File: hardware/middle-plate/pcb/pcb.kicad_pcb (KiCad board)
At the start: 2 copper layers, 218 x 205.7 mm, 101 parts, among them J1 Conn_01x06, J2 Conn_01x06, J3 Conn_01x05, J4 Conn_01x04, SW1 MT-0-102-A101-M200-RS+PJ, SW10 TS4535TP 250GF 009, SW11 TS4535TP 250GF 009, SW2 TS4535TP 250GF 009, SW3 TS4535TP 250GF 009, SW4 TS4535TP 250GF 009, SW5 TS4535TP 250GF 009, SW6 TS4535TP 250GF 009, SW7 TS4535TP 250GF 009, SW8 TS4535TP 250GF 009, SW9 TS4535TP 250GF 009, U1 Pico, U2 RPi_Zero_2W, U3 SN74LVC1T45DBV, U4 MAX98357_breakout

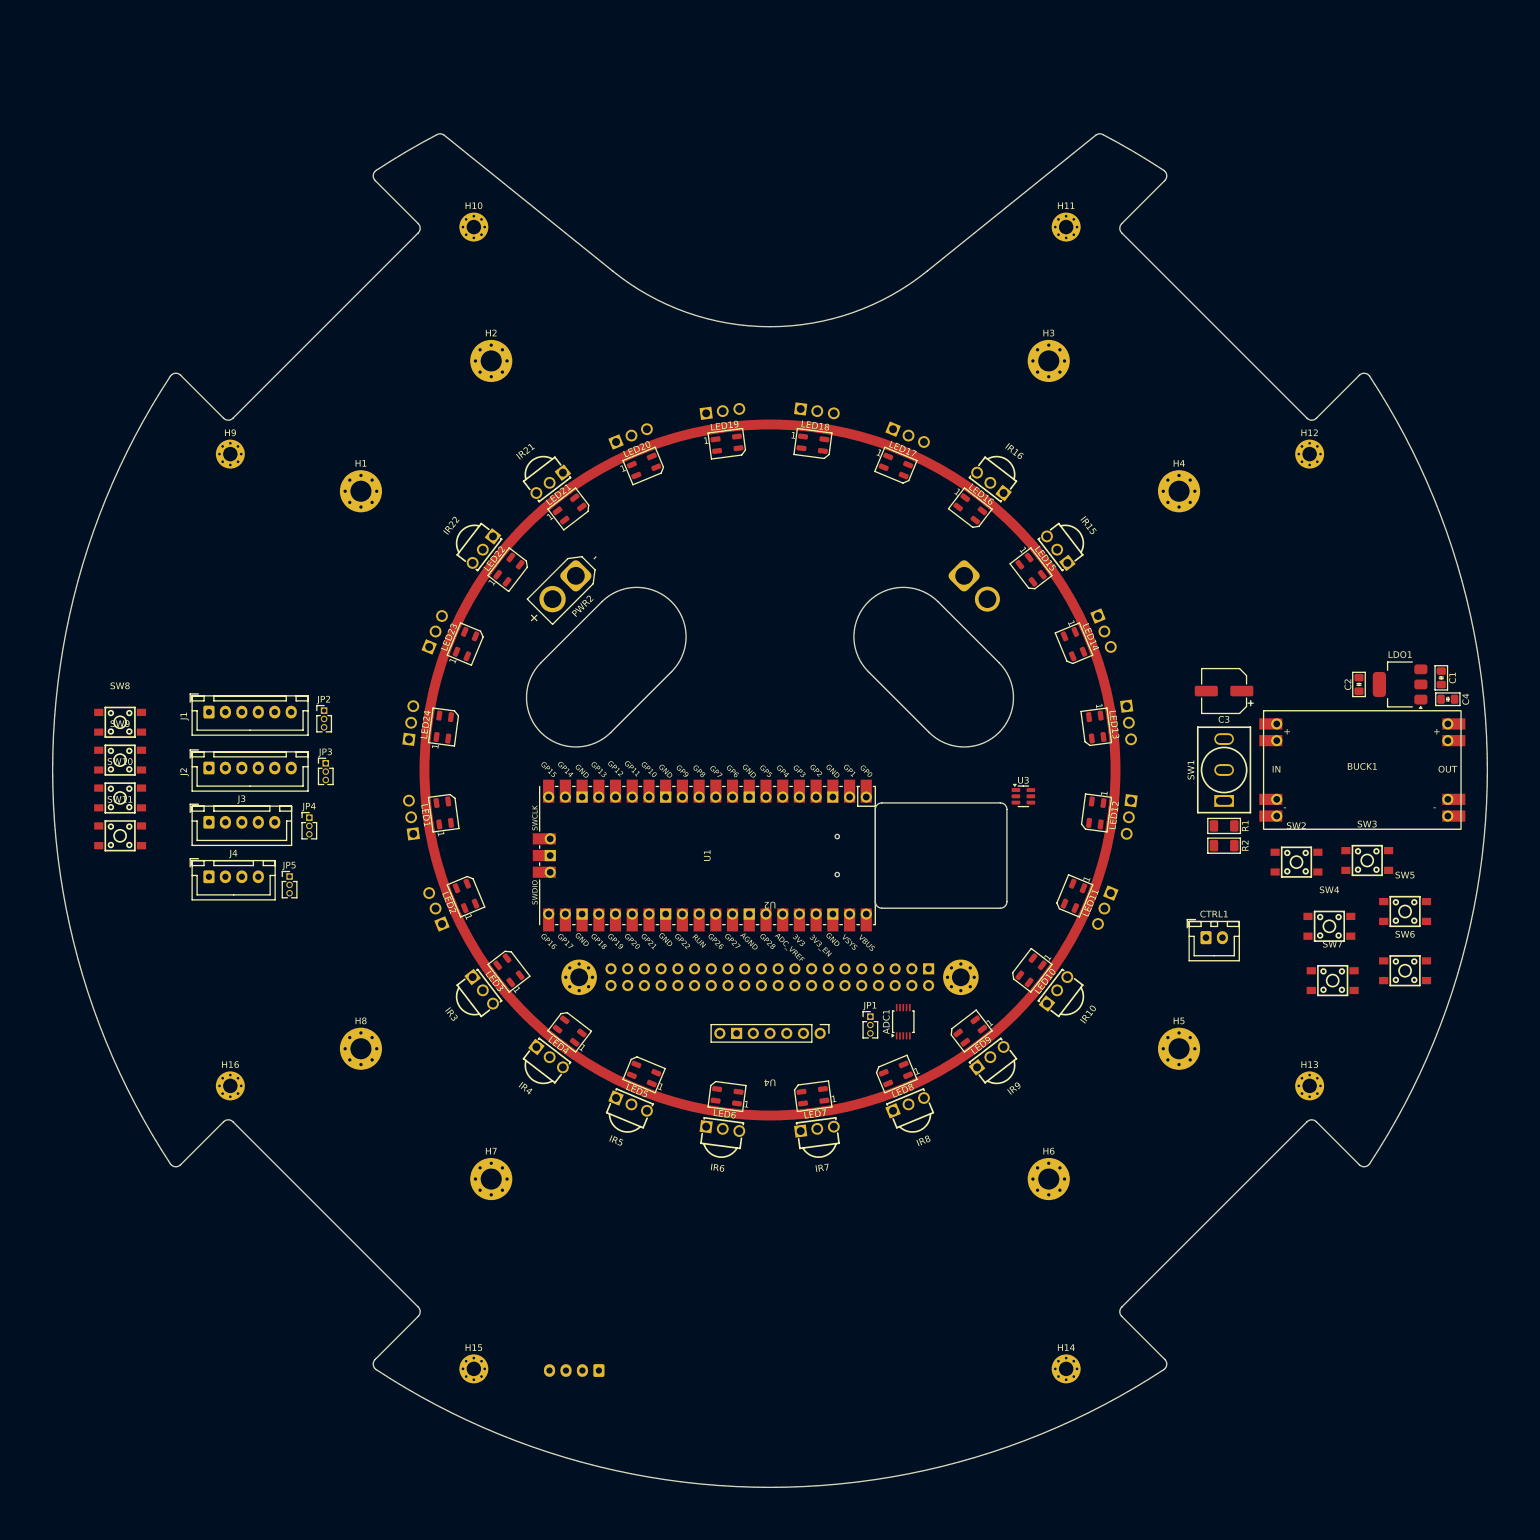
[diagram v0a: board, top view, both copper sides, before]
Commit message: middle plate completed other than cutouts
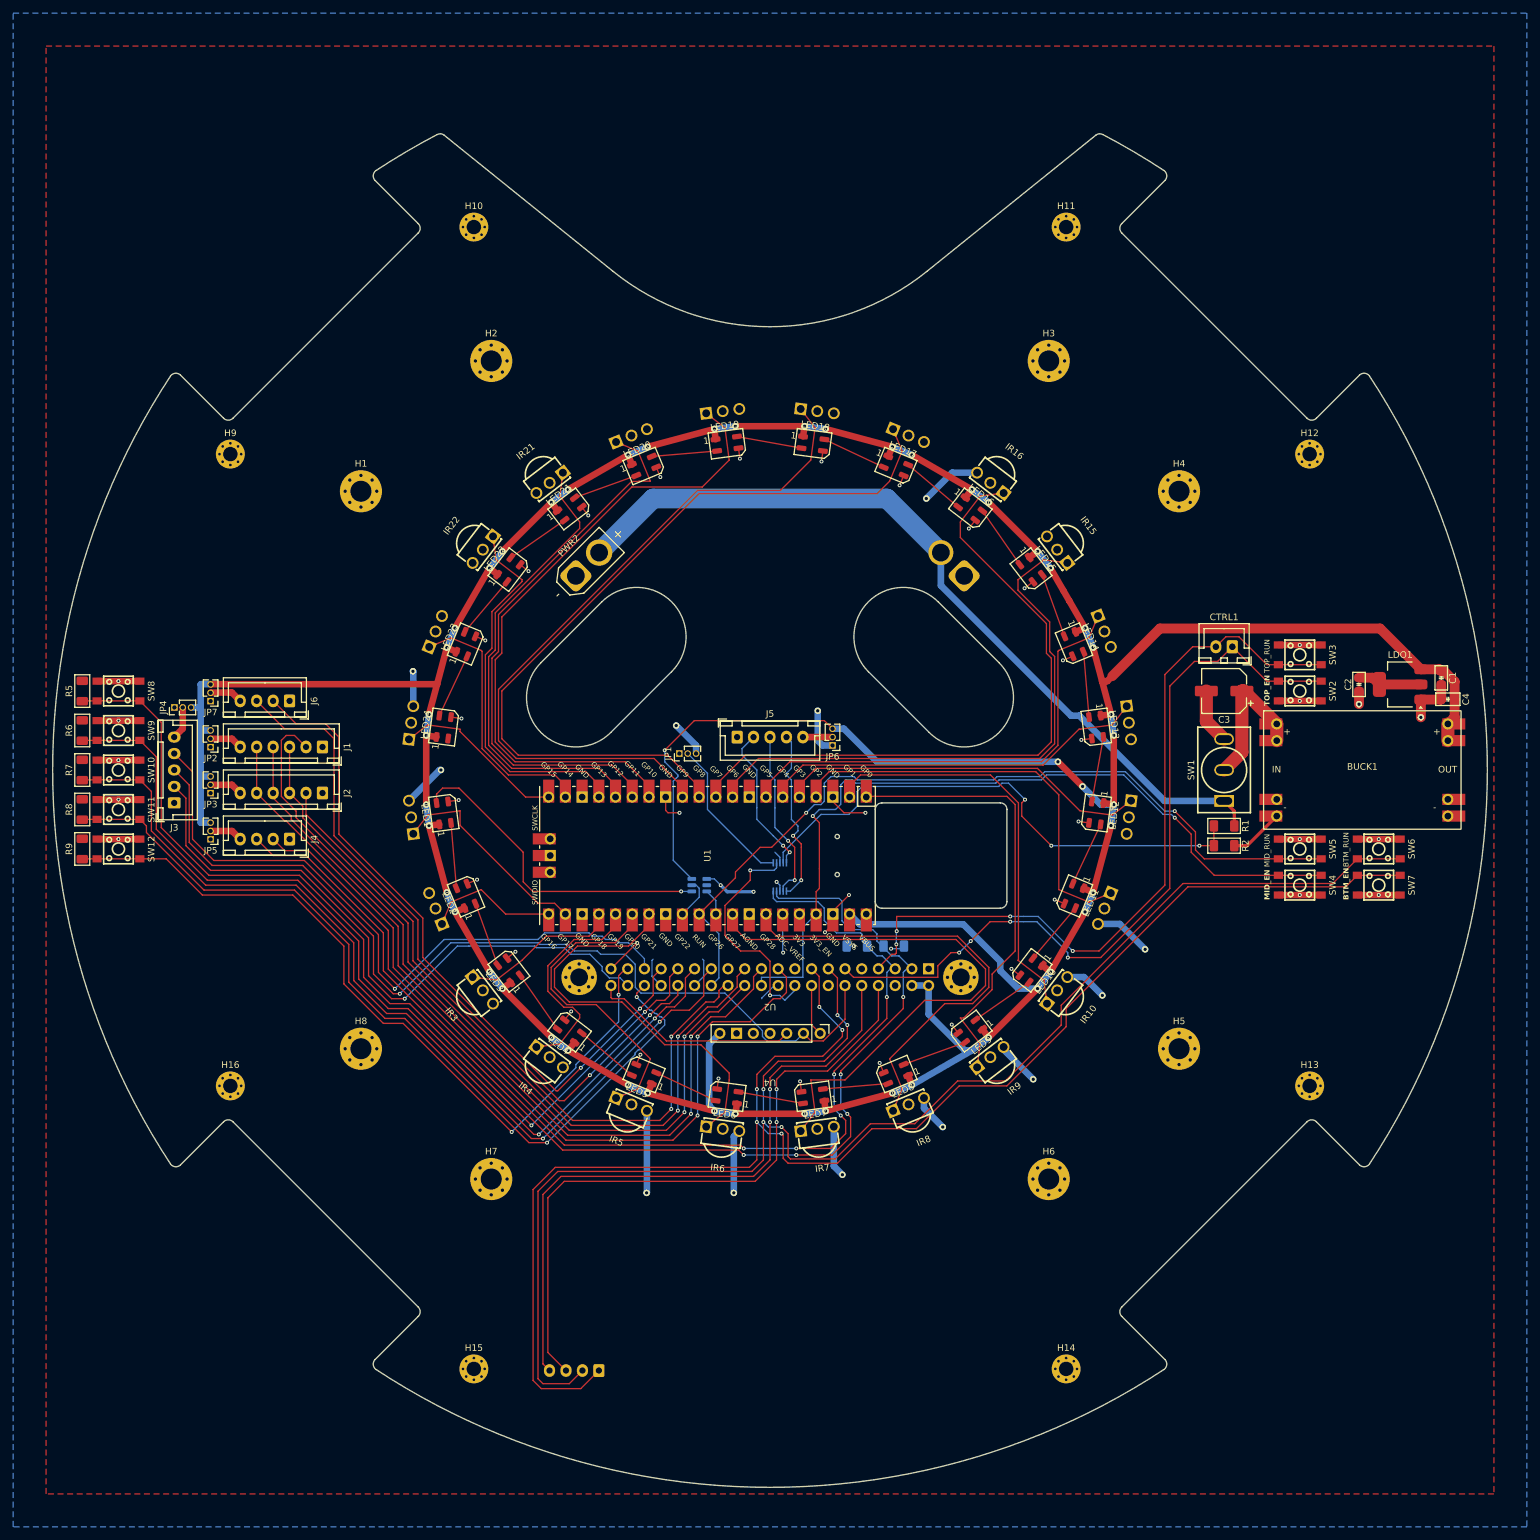
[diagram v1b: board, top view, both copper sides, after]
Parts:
- added J5: Conn_01x05, Connector_JST:JST_XH_B5B-XH-A_1x05_P2.50mm_Vertical, F.Cu at (-5.00, -5.00)
- added J6: Conn_01x04, Connector_JST:JST_XH_B4B-XH-A_1x04_P2.50mm_Vertical, F.Cu at (-73.0, -10.5)
- added JP6: Jumper_3_Bridged12, Connector_PinHeader_1.27mm:PinHeader_1x03_P1.27mm_Vertical, F.Cu at (9.50, -3.73)
- added JP7: Jumper_3_Bridged12, Connector_PinHeader_1.27mm:PinHeader_1x03_P1.27mm_Vertical, F.Cu at (-85.0, -10.5)
- added R3: 2.7kR, PCM_Resistor_SMD_AKL:R_1206_3216Metric_Pad1.30x1.75mm_HandSolder, B.Cu at (18.8, 26.8)
- added R4: 2.7kR, PCM_Resistor_SMD_AKL:R_1206_3216Metric_Pad1.30x1.75mm_HandSolder, B.Cu at (13.2, 26.8)
- added R5: 10kR, PCM_Resistor_SMD_AKL:R_1206_3216Metric_Pad1.30x1.75mm_HandSolder, F.Cu at (-104.5, -12.0)
- added R6: 10kR, PCM_Resistor_SMD_AKL:R_1206_3216Metric_Pad1.30x1.75mm_HandSolder, F.Cu at (-104.5, -6.00)
- added R7: 10kR, PCM_Resistor_SMD_AKL:R_1206_3216Metric_Pad1.30x1.75mm_HandSolder, F.Cu at (-104.5, 0.00)
- added R8: 10kR, PCM_Resistor_SMD_AKL:R_1206_3216Metric_Pad1.30x1.75mm_HandSolder, F.Cu at (-104.5, 6.00)
- added R9: 10kR, PCM_Resistor_SMD_AKL:R_1206_3216Metric_Pad1.30x1.75mm_HandSolder, F.Cu at (-104.5, 12.0)
- added SW12: TS4535TP 250GF 009, EasyEDA:SW-SMD_4P-L4.5-W4.5-P3.00-LS6.8, F.Cu at (-99.0, 12.0)
- ADC1, U3: moved to B.Cu
- moved U3 51.1 mm to (-10.8, 17.5), turned to 180 degrees
- moved JP1 49.4 mm to (-13.8, -2.50), turned to 90 degrees
- moved CTRL1 44.4 mm to (70.2, -18.7), turned to 180 degrees
- moved SW3 32.9 mm to (80.5, -17.5)
- moved ADC1 28.9 mm to (1.50, 16.2), turned to -90 degrees
- moved JP4 26.5 mm to (-90.5, -9.50), turned to 90 degrees
- moved SW2 26.0 mm to (80.5, -12.0), turned to 180 degrees
- moved SW6 18.9 mm to (92.5, 12.0)
- moved SW5 18.6 mm to (80.5, 12.0)
- moved JP2 18.1 mm to (-85.0, -3.48), turned to 180 degrees
- moved JP3 18.1 mm to (-85.0, 3.52), turned to 180 degrees
- moved J1 18.0 mm to (-68.0, -3.50), turned to 180 degrees
- moved J2 17.7 mm to (-68.0, 3.50), turned to 180 degrees
- moved SW7 16.1 mm to (92.5, 17.5), turned to 180 degrees
- moved J4 13.5 mm to (-73.0, 10.5), turned to 180 degrees
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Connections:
- net /PCM_CLK renamed /PCM.CLK
- net /PCM_DOUT renamed /PCM.DOUT
- ADC1 pad 10: /SCL -> /PI_I2C.SCL
- ADC1 pad 9: /SDA -> /PI_I2C.SDA
- CTRL1 pad 1: /EN -> /TOPPICO_TOGGLE.EN
- CTRL1 pad 2: /RUN -> /TOPPICO_TOGGLE.RUN
- CTRL2 pad 1: /RUN -> /BOTTOMPICO_TOGGLE.RUN
- CTRL2 pad 2: /EN -> /BOTTOMPICO_TOGGLE.EN
- CTRL2 pad 3: /RX -> /PI_UART.TX
- CTRL2 pad 4: /TX -> /PI_UART.RX
- J1 pad 2: /SPI0_MOSI -> /RPI_SPI0.SCS0
- J1 pad 3: /SPI0_MISO -> /RPI_SPI0.SCLK
- J1 pad 4: /SPI0_SCLK -> /RPI_SPI0.MISO
- J1 pad 5: /SPI0_CE0 -> /RPI_SPI0.MOSI
- J2 pad 2: /SPI0_MOSI -> /RPI_SPI0.SCS1
- J2 pad 3: /SPI0_MISO -> /RPI_SPI0.SCLK
- J2 pad 4: /SPI0_SCLK -> /RPI_SPI0.MISO
- J2 pad 5: /SPI0_CE1 -> /RPI_SPI0.MOSI
- J3 pad 2: /PCM_FS -> /PCM.DIN
- J3 pad 4: /PCM_DIN -> /PCM.FS
- J4 pad 2: /SDA -> /PI_I2C.SCL
- J4 pad 3: /SCL -> /PI_I2C.SDA
- SW2 pad 3: /BOTTOMPICO_EN -> /TOPPICO_TOGGLE.EN
- SW2 pad 4: /BOTTOMPICO_EN -> /TOPPICO_TOGGLE.EN
- SW3 pad 3: /BOTTOMPICO_RUN -> /TOPPICO_TOGGLE.RUN
- SW3 pad 4: /BOTTOMPICO_RUN -> /TOPPICO_TOGGLE.RUN
- SW4 pad 3: /MIDPICO_EN -> /MIDPICO_TOGGLE.EN
- SW4 pad 4: /MIDPICO_EN -> /MIDPICO_TOGGLE.EN
- SW5 pad 3: /MIDPICO_RUN -> /MIDPICO_TOGGLE.RUN
- SW5 pad 4: /MIDPICO_RUN -> /MIDPICO_TOGGLE.RUN
- SW6 pad 3: /TOPPICO_EN -> /BOTTOMPICO_TOGGLE.EN
- SW6 pad 4: /TOPPICO_EN -> /BOTTOMPICO_TOGGLE.EN
- SW7 pad 3: /TOPPICO_RUN -> /BOTTOMPICO_TOGGLE.RUN
- SW7 pad 4: /TOPPICO_RUN -> /BOTTOMPICO_TOGGLE.RUN
- U1 pad 1: /IR1 -> /IR9
- U1 pad 10: /IR8 -> /IR16
- U1 pad 11: /IR9 -> /IR17
- U1 pad 12: /IR10 -> /IR18
- U1 pad 14: /IR11 -> /IR19
- U1 pad 15: /IR12 -> /IR20
- U1 pad 16: /IR13 -> /IR21
- U1 pad 17: /IR14 -> /IR22
- U1 pad 19: /IR15 -> /IR23
- U1 pad 2: /IR2 -> /IR10
- U1 pad 20: /IR16 -> /IR24
- U1 pad 21: /LED_SIG_DIR -> /IR2
- U1 pad 22: /LED_SIG_3V3 -> /IR1
- U1 pad 24: /IR24 -> /IR3
- U1 pad 25: /IR23 -> /IR4
- U1 pad 26: /IR22 -> /IR5
- U1 pad 27: /IR21 -> /IR6
- U1 pad 29: /IR20 -> /LED_SIG_DIR
- U1 pad 30: /RUN -> /MIDPICO_TOGGLE.RUN
- U1 pad 31: /IR19 -> /LED_SIG_3V3
- U1 pad 32: /IR18 -> /IR7
- U1 pad 34: /IR17 -> /IR8
- U1 pad 37: /EN -> /MIDPICO_TOGGLE.EN
- U1 pad 4: /IR3 -> /IR11
- U1 pad 5: /IR4 -> /IR12
- U1 pad 6: /IR5 -> /IR13
- U1 pad 7: /IR6 -> /IR14
- U1 pad 9: /IR7 -> /IR15
- U2 pad 10: /RX -> /PI_UART.RX
- U2 pad 11: /BOTTOMPICO_EN -> /TOPPICO_TOGGLE.EN
- U2 pad 13: /BOTTOMPICO_RUN -> /BOTTOMPICO_TOGGLE.EN
- U2 pad 15: /PI_SW1 -> /BOTTOMPICO_TOGGLE.RUN
- U2 pad 16: /TOPPICO_EN -> /LRC
- U2 pad 17: +3V3 -> unconnected-(U2-3V3-Pad17)
- U2 pad 18: /TOPPICO_RUN -> /ADC_INT
- U2 pad 19: /SPI0_MOSI -> /RPI_SPI0.MOSI
- U2 pad 21: /SPI0_MISO -> /RPI_SPI0.MISO
- U2 pad 22: /MIDPICO_EN -> /MIDPICO_TOGGLE.EN
- U2 pad 23: /SPI0_SCLK -> /RPI_SPI0.SCLK
- U2 pad 24: /SPI0_CE0 -> /RPI_SPI0.SCS0
- U2 pad 26: /SPI0_CE1 -> /RPI_SPI0.SCS1
- U2 pad 27: /PI_SW2 -> /PI_SW3
- U2 pad 28: /MIDPICO_RUN -> /MIDPICO_TOGGLE.RUN
- U2 pad 29: /PI_SW3 -> /PI_SW2
- U2 pad 3: /SDA -> /PI_I2C.SDA
- U2 pad 31: /PI_SW4 -> /PI_SW1
- U2 pad 35: /PCM_FS -> /PCM.FS
- U2 pad 36: /LED_SIG_DIR -> /PI_SW4
- U2 pad 37: /LRC -> /PI_SW5
- U2 pad 38: /PCM_DIN -> /PCM.DIN
- U2 pad 5: /SCL -> /PI_I2C.SCL
- U2 pad 7: unconnected-(U2-GP4(GPCLK0)-Pad7) -> /TOPPICO_TOGGLE.RUN
- U2 pad 8: /TX -> /PI_UART.TX
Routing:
- net +5V: track 0.00 -> 661.5 mm, vias 0 -> 50
- net /BOTTOMPICO_TOGGLE.RUN: track 0.00 -> 239.3 mm, vias 0 -> 5
- net /BOTTOMPICO_TOGGLE.EN: track 0.00 -> 234.0 mm, vias 0 -> 5
- net GND: track 0.00 -> 174.9 mm, vias 0 -> 42
- net /PI_I2C.SDA: track 0.00 -> 174.0 mm, vias 0 -> 5
- net /PI_I2C.SCL: track 0.00 -> 166.6 mm, vias 0 -> 5
- net /PCM.CLK: track 0.00 -> 143.9 mm, vias 0 -> 1
- net /PI_SW1: track 0.00 -> 141.5 mm, vias 0 -> 2
- net /PI_SW2: track 0.00 -> 139.7 mm, vias 0 -> 2
- net /PI_SW3: track 0.00 -> 137.5 mm, vias 0 -> 2
- net /RPI_SPI0.MOSI: track 0.00 -> 133.3 mm, vias 0 -> 2
- net /PI_SW4: track 0.00 -> 129.1 mm, vias 0 -> 2
- net /MIDPICO_TOGGLE.RUN: track 0.00 -> 125.7 mm, vias 0 -> 2
- net /RPI_SPI0.MISO: track 0.00 -> 125.4 mm, vias 0 -> 2
- net VCC: track 0.00 -> 124.8 mm
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- added copper zone on F.Cu, net +3V3
- added copper zone on B.Cu, net GND
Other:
- board text added: "BTM_EN"
- board text added: "BTM_RUN"
- board text added: "MID_EN"
- board text added: "MID_RUN"
- board text added: "TOP_EN"
- board text added: "TOP_RUN"

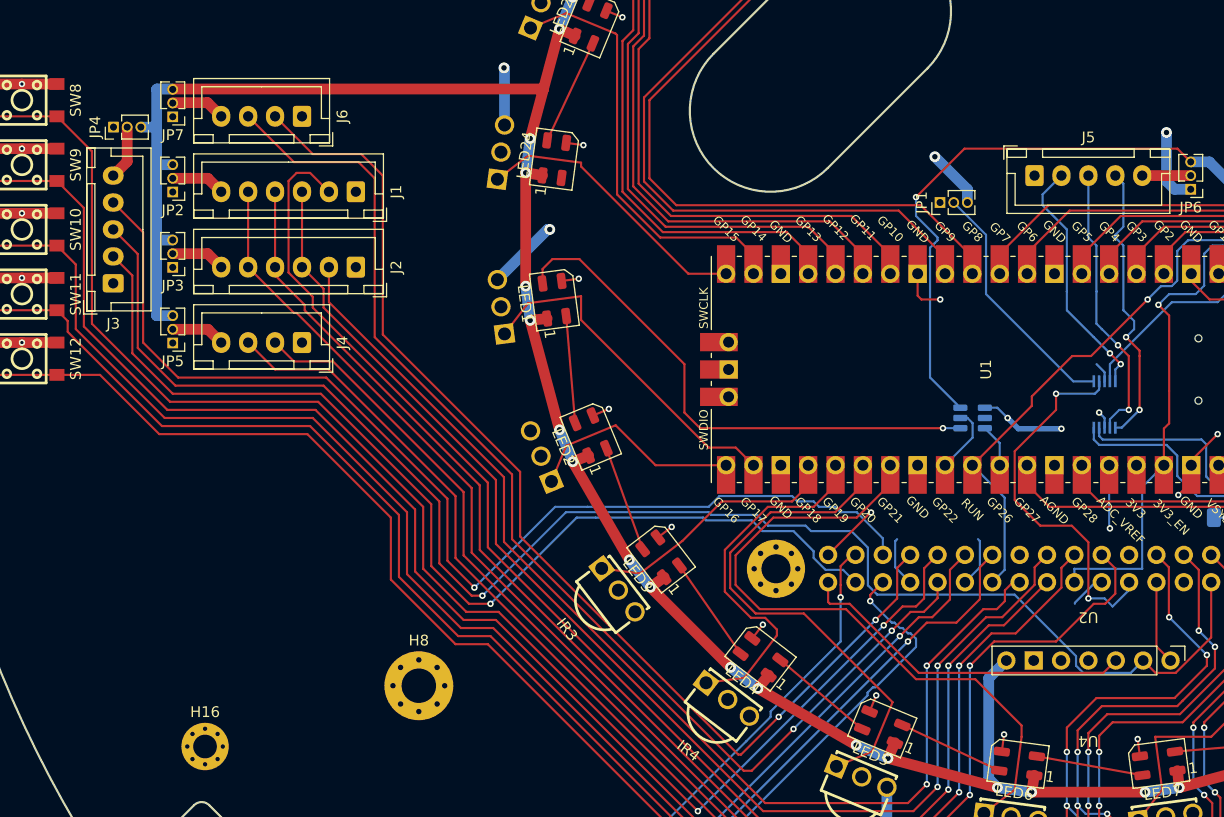
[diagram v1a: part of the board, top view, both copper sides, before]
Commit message: changed some reference designators, and cleaned up schematics
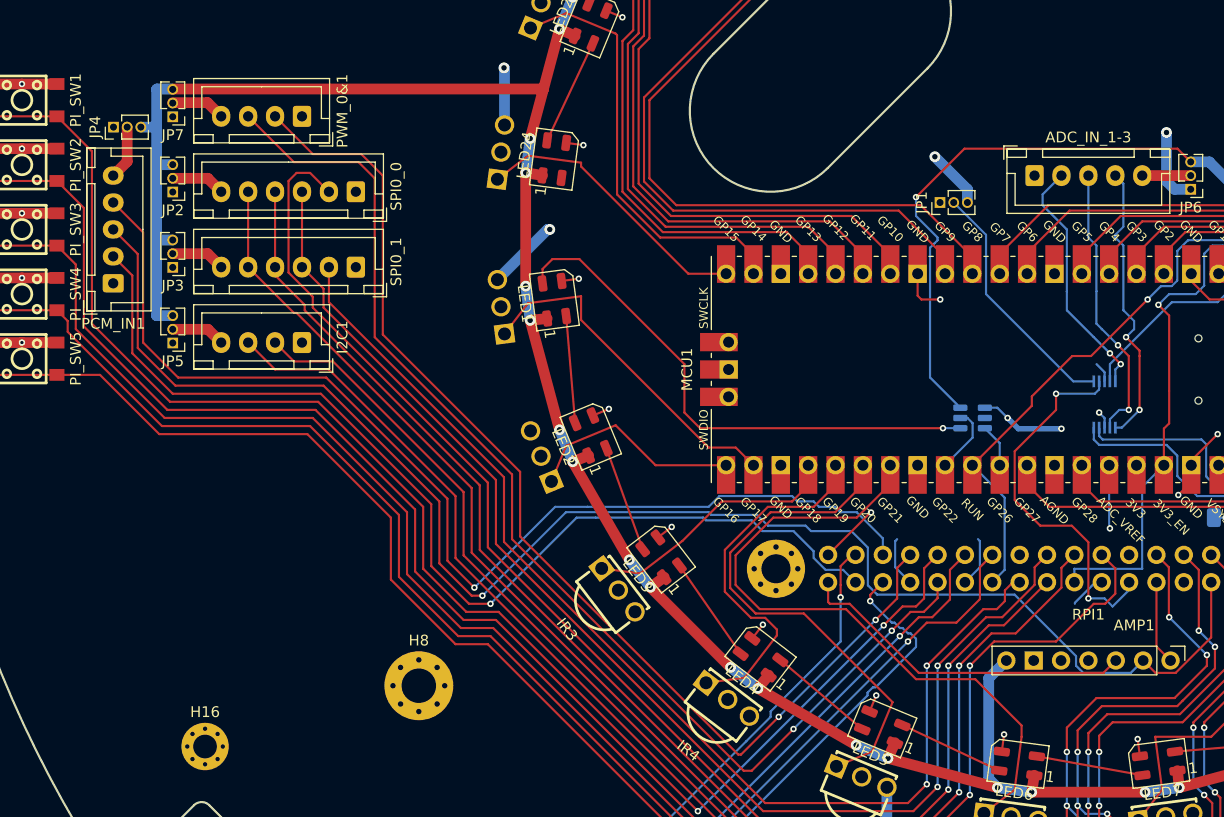
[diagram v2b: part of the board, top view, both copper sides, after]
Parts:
- renumbered J5 to ADC_IN_1-3, U4 to AMP1, J4 to I2C1, U3 to LVL1, U1 to MCU1, J3 to PCM_IN1, SW8 to PI_SW1, SW9 to PI_SW2, SW10 to PI_SW3, SW11 to PI_SW4, SW12 to PI_SW5, J6 to PWM_0&1, U2 to RPI1, J1 to SPI0_0, J2 to SPI0_1
